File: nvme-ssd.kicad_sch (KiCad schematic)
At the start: 20 parts, among them J3 1-2199230-6

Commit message: Update D1, D11 symbol
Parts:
- D1: symbol antmicroLEDIndicationDiscrete:598-8D80-107F -> antmicroLEDIndicationDiscrete:LED_R_0603_598-8D80-107F
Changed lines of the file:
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@@
     (pin "2")
   )
-  (symbol (lib_id "antmicroLEDIndicationDiscrete:598-8D80-107F") (at 118.11 123.19 0) (unit 1)
+  (symbol (lib_id "antmicroLEDIndicationDiscrete:LED_R_0603_598-8D80-107F") (at 118.11 123.19 0) (unit 1)
     (in_bom yes) (on_board yes)
     (property "Reference" "D1" (id 0) (at 116.84 128.27 90)
@@
       (effects (font (size 1.27 1.27) (thickness 0.15)) (justify left bottom) hide)
     )
-    (property "Datasheet" "" (id 3) (at 140.97 133.35 0)
+    (property "Datasheet" "https://www.farnell.com/datasheets/3093797.pdf" (id 3) (at 140.97 133.35 0)
       (effects (font (size 1.27 1.27) (thickness 0.15)) (justify left bottom) hide)
     )

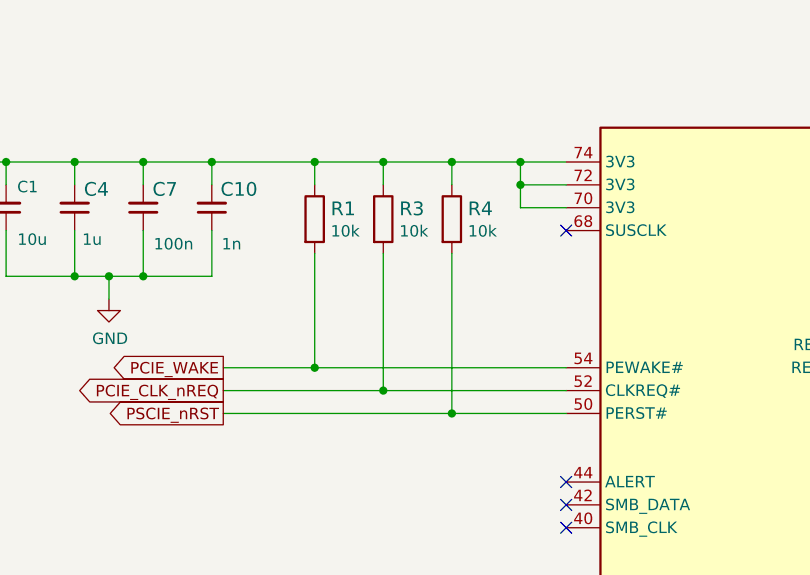
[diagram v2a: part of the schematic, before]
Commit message: Update R1, R3, R4 symbol and footprint
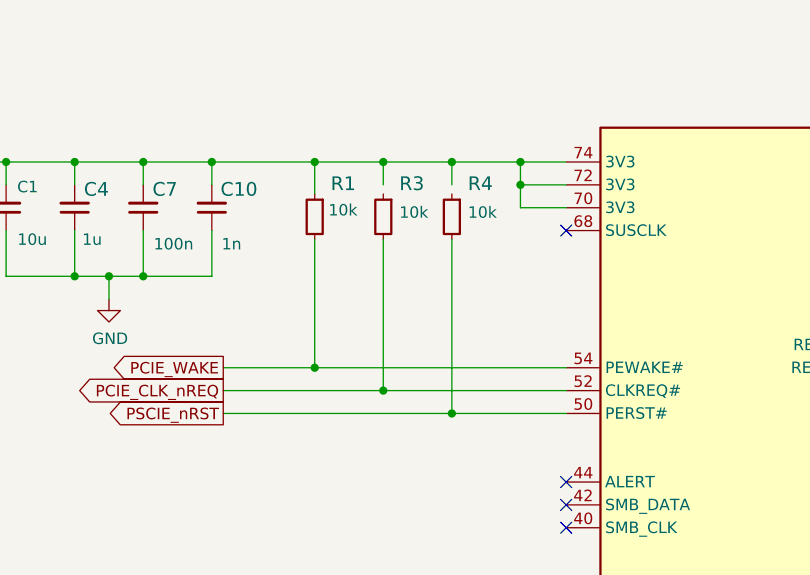
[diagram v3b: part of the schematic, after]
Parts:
- R1, R3, R4: footprint scalenode-cm4-baseboard-footprints:0603-res -> antmicro-footprints:R_0603_1608Metric; symbol scalenode-cm4-baseboard:R_10k_0603 -> antmicroResistors0603:R_10k_0603; Author (none) -> Antmicro; License (none) -> Apache-2.0; MPN CR0603-JW-103ELF -> CR0603-FX-1002ELF; Manufacturer BOURNS -> Bourns; Tolerance (none) -> 1%
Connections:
- net 3V3_SSD: no longer R3.1, R4.1
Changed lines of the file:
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@@
     (stroke (width 0) (type default) (color 0 0 0 0))
   )
-  (wire (pts (xy 105.41 46.99) (xy 105.41 44.45))
+  (wire (pts (xy 105.41 44.45) (xy 105.41 48.006))
     (stroke (width 0) (type default) (color 0 0 0 0))
   )
@@
     (stroke (width 0) (type default) (color 0 0 0 0))
   )
-  (wire (pts (xy 113.03 54.61) (xy 113.03 69.85))
-    (stroke (width 0) (type default) (color 0 0 0 0))
-  )
   (wire (pts (xy 82.55 125.73) (xy 86.36 125.73))
     (stroke (width 0) (type default) (color 0 0 0 0))
@@
     (stroke (width 0) (type default) (color 0 0 0 0))
   )
+  (wire (pts (xy 105.41 53.086) (xy 105.41 67.31))
+    (stroke (width 0) (type default) (color 0 0 0 0))
+  )
   (wire (pts (xy 171.45 115.57) (xy 181.61 115.57))
     (stroke (width 0) (type default) (color 0 0 0 0))
@@
     (stroke (width 0) (type default) (color 0 0 0 0))
   )
+  (wire (pts (xy 120.65 53.086) (xy 120.65 72.39))
+    (stroke (width 0) (type default) (color 0 0 0 0))
+  )
   (wire (pts (xy 128.27 113.03) (xy 106.68 113.03))
     (stroke (width 0) (type default) (color 0 0 0 0))
@@
     (stroke (width 0) (type default) (color 0 0 0 0))
   )
-  (wire (pts (xy 105.41 54.61) (xy 105.41 67.31))
-    (stroke (width 0) (type default) (color 0 0 0 0))
-  )
   (wire (pts (xy 181.61 92.71) (xy 181.61 100.33))
     (stroke (width 0) (type default) (color 0 0 0 0))
@@
     (stroke (width 0) (type default) (color 0 0 0 0))
   )
-  (wire (pts (xy 120.65 54.61) (xy 120.65 72.39))
-    (stroke (width 0) (type default) (color 0 0 0 0))
-  )
   (wire (pts (xy 128.27 118.11) (xy 128.27 115.57))
     (stroke (width 0) (type default) (color 0 0 0 0))
@@
   )
   (wire (pts (xy 171.45 130.81) (xy 181.61 130.81))
+    (stroke (width 0) (type default) (color 0 0 0 0))
+  )
+  (wire (pts (xy 113.03 53.086) (xy 113.03 69.85))
     (stroke (width 0) (type default) (color 0 0 0 0))
   )
@@
     (pin "1")
   )
-  (symbol (lib_id "scalenode-cm4-baseboard:R_10k_0603") (at 113.03 50.8 270) (unit 1)
+  (symbol (lib_id "antmicroResistors0603:R_10k_0603") (at 113.03 48.006 270) (unit 1)
     (in_bom yes) (on_board yes)
-    (property "Reference" "R3" (id 0) (at 114.808 49.657 90)
+    (property "Reference" "R3" (id 0) (at 114.808 46.863 90)
       (effects (font (size 1.524 1.524)) (justify left))
     )
-    (property "Value" "R_10k_0603" (id 1) (at 109.22 50.8 0)
+    (property "Value" "R_10k_0603" (id 1) (at 109.22 48.006 0)
       (effects (font (size 1.524 1.524)) hide)
     )
-    (property "Footprint" "scalenode-cm4-baseboard-footprints:0603-res" (id 2) (at 118.11 55.88 0)
-      (effects (font (size 1.524 1.524)) (justify left) hide)
-    )
-    (property "Datasheet" "" (id 3) (at 113.03 50.8 0)
-      (effects (font (size 1.27 1.27)) hide)
-    )
-    (property "Manufacturer" "BOURNS" (id 4) (at 123.19 55.88 0)
-      (effects (font (size 1.524 1.524)) (justify left) hide)
-    )
-    (property "MPN" "CR0603-JW-103ELF" (id 5) (at 120.65 55.88 0)
-      (effects (font (size 1.524 1.524)) (justify left) hide)
-    )
-    (property "Val" "10k" (id 6) (at 114.808 52.1462 90)
-      (effects (font (size 1.27 1.27)) (justify left))
+    (property "Footprint" "antmicro-footprints:R_0603_1608Metric" (id 2) (at 97.79 68.326 0)
+      (effects (font (size 1.27 1.27) (thickness 0.15)) (justify left bottom) hide)
+    )
+    (property "Datasheet" "https://www.bourns.com/docs/product-datasheets/cr.pdf" (id 3) (at 95.25 68.326 0)
+      (effects (font (size 1.27 1.27) (thickness 0.15)) (justify left bottom) hide)
+    )
+    (property "Manufacturer" "Bourns" (id 4) (at 90.17 68.326 0)
+      (effects (font (size 1.27 1.27) (thickness 0.15)) (justify left bottom) hide)
+    )
+    (property "MPN" "CR0603-FX-1002ELF" (id 5) (at 92.71 68.326 0)
+      (effects (font (size 1.27 1.27) (thickness 0.15)) (justify left bottom) hide)
+    )
+    (property "Val" "10k" (id 6) (at 114.808 50.8 90)
+      (effects (font (size 1.27 1.27) (thickness 0.15)) (justify left bottom))
+    )
+    (property "License" "Apache-2.0" (id 7) (at 87.63 68.326 0)
+      (effects (font (size 1.27 1.27) (thickness 0.15)) (justify left bottom) hide)
+    )
+    (property "Author" "Antmicro" (id 8) (at 85.09 68.326 0)
+      (effects (font (size 1.27 1.27) (thickness 0.15)) (justify left bottom) hide)
+    )
+    (property "Tolerance" "1%" (id 9) (at 102.87 68.326 0)
+      (effects (font (size 1.27 1.27)) (justify left bottom) hide)
     )
     (pin "1")
     (pin "2")
   )
-  (symbol (lib_id "scalenode-cm4-baseboard:R_10k_0603") (at 120.65 50.8 270) (unit 1)
+  (symbol (lib_id "antmicroResistors0603:R_10k_0603") (at 120.65 48.006 270) (unit 1)
     (in_bom yes) (on_board yes)
-    (property "Reference" "R4" (id 0) (at 122.428 49.657 90)
+    (property "Reference" "R4" (id 0) (at 122.428 46.863 90)
       (effects (font (size 1.524 1.524)) (justify left))
     )
-    (property "Value" "R_10k_0603" (id 1) (at 116.84 50.8 0)
+    (property "Value" "R_10k_0603" (id 1) (at 116.84 48.006 0)
       (effects (font (size 1.524 1.524)) hide)
     )
-    (property "Footprint" "scalenode-cm4-baseboard-footprints:0603-res" (id 2) (at 125.73 55.88 0)
-      (effects (font (size 1.524 1.524)) (justify left) hide)
-    )
-    (property "Datasheet" "" (id 3) (at 120.65 50.8 0)
-      (effects (font (size 1.27 1.27)) hide)
-    )
-    (property "Manufacturer" "BOURNS" (id 4) (at 130.81 55.88 0)
-      (effects (font (size 1.524 1.524)) (justify left) hide)
-    )
-    (property "MPN" "CR0603-JW-103ELF" (id 5) (at 128.27 55.88 0)
-      (effects (font (size 1.524 1.524)) (justify left) hide)
-    )
-    (property "Val" "10k" (id 6) (at 122.428 52.1462 90)
-      (effects (font (size 1.27 1.27)) (justify left))
+    (property "Footprint" "antmicro-footprints:R_0603_1608Metric" (id 2) (at 105.41 68.326 0)
+      (effects (font (size 1.27 1.27) (thickness 0.15)) (justify left bottom) hide)
+    )
+    (property "Datasheet" "https://www.bourns.com/docs/product-datasheets/cr.pdf" (id 3) (at 102.87 68.326 0)
+      (effects (font (size 1.27 1.27) (thickness 0.15)) (justify left bottom) hide)
+    )
+    (property "Manufacturer" "Bourns" (id 4) (at 97.79 68.326 0)
+      (effects (font (size 1.27 1.27) (thickness 0.15)) (justify left bottom) hide)
+    )
+    (property "MPN" "CR0603-FX-1002ELF" (id 5) (at 100.33 68.326 0)
+      (effects (font (size 1.27 1.27) (thickness 0.15)) (justify left bottom) hide)
+    )
+    (property "Val" "10k" (id 6) (at 122.428 50.8 90)
+      (effects (font (size 1.27 1.27) (thickness 0.15)) (justify left bottom))
+    )
+    (property "License" "Apache-2.0" (id 7) (at 95.25 68.326 0)
+      (effects (font (size 1.27 1.27) (thickness 0.15)) (justify left bottom) hide)
+    )
+    (property "Author" "Antmicro" (id 8) (at 92.71 68.326 0)
+      (effects (font (size 1.27 1.27) (thickness 0.15)) (justify left bottom) hide)
+    )
+    (property "Tolerance" "1%" (id 9) (at 110.49 68.326 0)
+      (effects (font (size 1.27 1.27)) (justify left bottom) hide)
     )
     (pin "1")
     (pin "2")
   )
-  (symbol (lib_id "scalenode-cm4-baseboard:R_10k_0603") (at 105.41 50.8 270) (unit 1)
+  (symbol (lib_id "antmicroResistors0603:R_10k_0603") (at 105.41 48.006 270) (unit 1)
     (in_bom yes) (on_board yes)
-    (property "Reference" "R1" (id 0) (at 107.188 49.657 90)
+    (property "Reference" "R1" (id 0) (at 107.188 46.863 90)
       (effects (font (size 1.524 1.524)) (justify left))
     )
-    (property "Value" "R_10k_0603" (id 1) (at 101.6 50.8 0)
+    (property "Value" "R_10k_0603" (id 1) (at 101.6 48.006 0)
       (effects (font (size 1.524 1.524)) hide)
     )
-    (property "Footprint" "scalenode-cm4-baseboard-footprints:0603-res" (id 2) (at 110.49 55.88 0)
-      (effects (font (size 1.524 1.524)) (justify left) hide)
-    )
-    (property "Datasheet" "" (id 3) (at 105.41 50.8 0)
-      (effects (font (size 1.27 1.27)) hide)
-    )
-    (property "Manufacturer" "BOURNS" (id 4) (at 115.57 55.88 0)
-      (effects (font (size 1.524 1.524)) (justify left) hide)
-    )
-    (property "MPN" "CR0603-JW-103ELF" (id 5) (at 113.03 55.88 0)
-      (effects (font (size 1.524 1.524)) (justify left) hide)
-    )
-    (property "Val" "10k" (id 6) (at 107.188 52.1462 90)
-      (effects (font (size 1.27 1.27)) (justify left))
+    (property "Footprint" "antmicro-footprints:R_0603_1608Metric" (id 2) (at 90.17 68.326 0)
+      (effects (font (size 1.27 1.27) (thickness 0.15)) (justify left bottom) hide)
+    )
+    (property "Datasheet" "https://www.bourns.com/docs/product-datasheets/cr.pdf" (id 3) (at 87.63 68.326 0)
+      (effects (font (size 1.27 1.27) (thickness 0.15)) (justify left bottom) hide)
+    )
+    (property "Manufacturer" "Bourns" (id 4) (at 82.55 68.326 0)
+      (effects (font (size 1.27 1.27) (thickness 0.15)) (justify left bottom) hide)
+    )
+    (property "MPN" "CR0603-FX-1002ELF" (id 5) (at 85.09 68.326 0)
+      (effects (font (size 1.27 1.27) (thickness 0.15)) (justify left bottom) hide)
+    )
+    (property "Val" "10k" (id 6) (at 106.934 50.546 90)
+      (effects (font (size 1.27 1.27) (thickness 0.15)) (justify left bottom))
+    )
+    (property "License" "Apache-2.0" (id 7) (at 80.01 68.326 0)
+      (effects (font (size 1.27 1.27) (thickness 0.15)) (justify left bottom) hide)
+    )
+    (property "Author" "Antmicro" (id 8) (at 77.47 68.326 0)
+      (effects (font (size 1.27 1.27) (thickness 0.15)) (justify left bottom) hide)
+    )
+    (property "Tolerance" "1%" (id 9) (at 95.25 68.326 0)
+      (effects (font (size 1.27 1.27)) (justify left bottom) hide)
     )
     (pin "1")

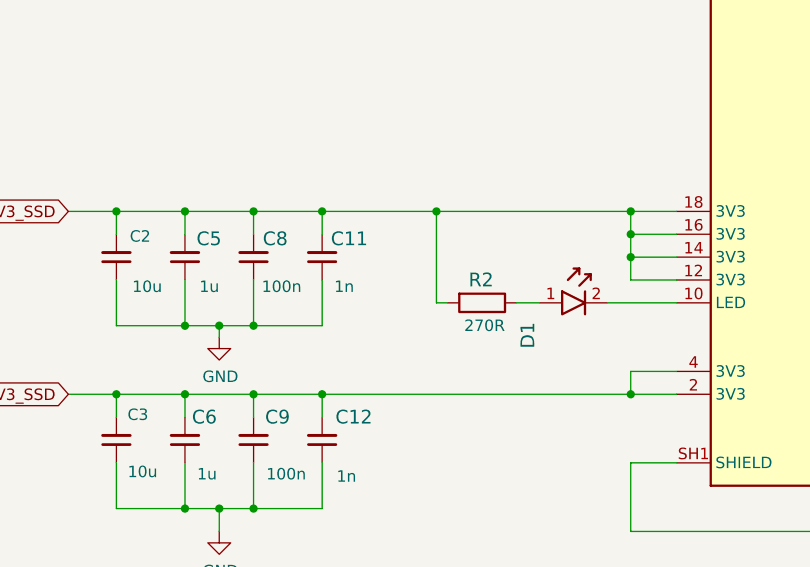
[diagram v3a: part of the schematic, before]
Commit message: Update R2 symbol and footprint
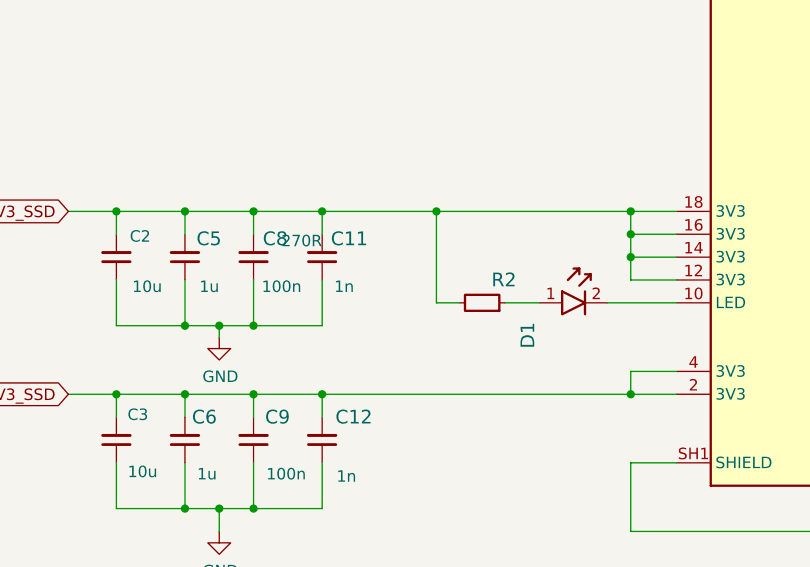
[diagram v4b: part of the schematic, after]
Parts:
- R2: footprint scalenode-cm4-baseboard-footprints:0603-res -> antmicro-footprints:R_0603_1608Metric; symbol scalenode-cm4-baseboard:R_270R_0603 -> antmicroResistors0603:R_270R_0603; Author (none) -> Antmicro; License (none) -> Apache-2.0; MPN CRGH0603F270R -> CR0603-FX-2700ELF; Manufacturer TE_CONNECTIVITY -> Bourns; Tolerance (none) -> 1%
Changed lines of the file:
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@@
     (stroke (width 0) (type default) (color 0 0 0 0))
   )
-  (wire (pts (xy 107.95 123.19) (xy 106.68 123.19))
+  (wire (pts (xy 106.68 123.19) (xy 109.22 123.19))
     (stroke (width 0) (type default) (color 0 0 0 0))
   )
@@
     (stroke (width 0) (type default) (color 0 0 0 0))
   )
-  (wire (pts (xy 115.57 123.19) (xy 118.11 123.19))
+  (wire (pts (xy 114.3 123.19) (xy 118.11 123.19))
     (stroke (width 0) (type default) (color 0 0 0 0))
   )
@@
     (pin "SH2")
   )
-  (symbol (lib_id "scalenode-cm4-baseboard:R_270R_0603") (at 111.76 123.19 180) (unit 1)
+  (symbol (lib_id "antmicroResistors0603:R_270R_0603") (at 114.3 123.19 180) (unit 1)
     (in_bom yes) (on_board yes)
-    (property "Reference" "R2" (id 0) (at 113.03 120.65 0)
+    (property "Reference" "R2" (id 0) (at 115.57 120.65 0)
       (effects (font (size 1.524 1.524)) (justify left))
     )
-    (property "Value" "R_270R_0603" (id 1) (at 111.76 119.38 0)
+    (property "Value" "R_270R_0603" (id 1) (at 114.3 119.38 0)
       (effects (font (size 1.524 1.524)) hide)
     )
-    (property "Footprint" "scalenode-cm4-baseboard-footprints:0603-res" (id 2) (at 106.68 128.27 0)
-      (effects (font (size 1.524 1.524)) (justify left) hide)
+    (property "Footprint" "antmicro-footprints:R_0603_1608Metric" (id 2) (at 93.98 107.95 0)
+      (effects (font (size 1.27 1.27) (thickness 0.15)) (justify left bottom) hide)
     )
-    (property "Datasheet" "" (id 3) (at 111.76 123.19 0)
-      (effects (font (size 1.27 1.27)) hide)
+    (property "Datasheet" "https://www.bourns.com/docs/product-datasheets/cr.pdf" (id 3) (at 93.98 105.41 0)
+      (effects (font (size 1.27 1.27) (thickness 0.15)) (justify left bottom) hide)
+    )
+    (property "Manufacturer" "Bourns" (id 4) (at 93.98 100.33 0)
+      (effects (font (size 1.27 1.27) (thickness 0.15)) (justify left bottom) hide)
+    )
+    (property "MPN" "CR0603-FX-2700ELF" (id 5) (at 93.98 102.87 0)
+      (effects (font (size 1.27 1.27) (thickness 0.15)) (justify left bottom) hide)
+    )
+    (property "Val" "270R" (id 6) (at 93.98 115.57 0)
+      (effects (font (size 1.27 1.27) (thickness 0.15)) (justify left bottom))
     )
-    (property "Manufacturer" "TE_CONNECTIVITY" (id 4) (at 106.68 133.35 0)
-      (effects (font (size 1.524 1.524)) (justify left) hide)
+    (property "License" "Apache-2.0" (id 7) (at 93.98 97.79 0)
+      (effects (font (size 1.27 1.27) (thickness 0.15)) (justify left bottom) hide)
     )
-    (property "MPN" "CRGH0603F270R" (id 5) (at 106.68 130.81 0)
-      (effects (font (size 1.524 1.524)) (justify left) hide)
+    (property "Author" "Antmicro" (id 8) (at 93.98 95.25 0)
+      (effects (font (size 1.27 1.27) (thickness 0.15)) (justify left bottom) hide)
     )
-    (property "Val" "270R" (id 6) (at 114.3 125.73 0)
-      (effects (font (size 1.27 1.27)) (justify left))
+    (property "Tolerance" "1%" (id 9) (at 93.98 113.03 0)
+      (effects (font (size 1.27 1.27)) (justify left bottom) hide)
     )
     (pin "1")
